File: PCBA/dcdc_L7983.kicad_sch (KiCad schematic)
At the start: 13 parts

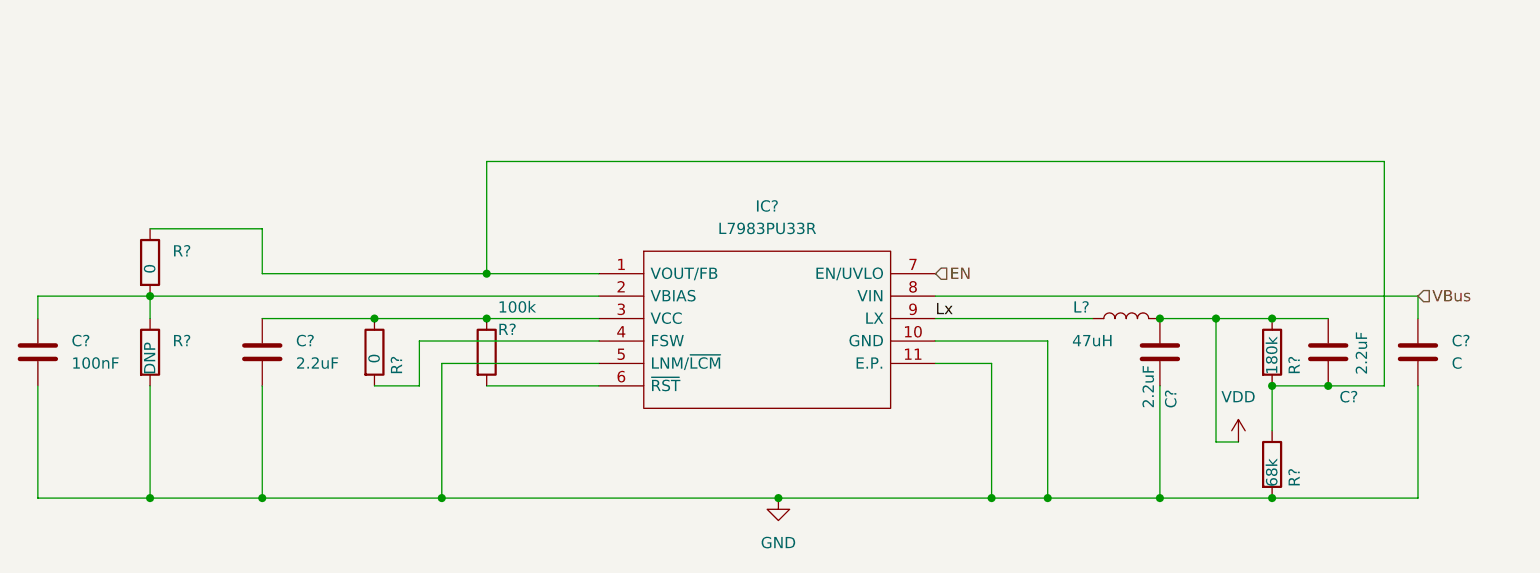
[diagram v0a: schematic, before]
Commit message: Assign footprints
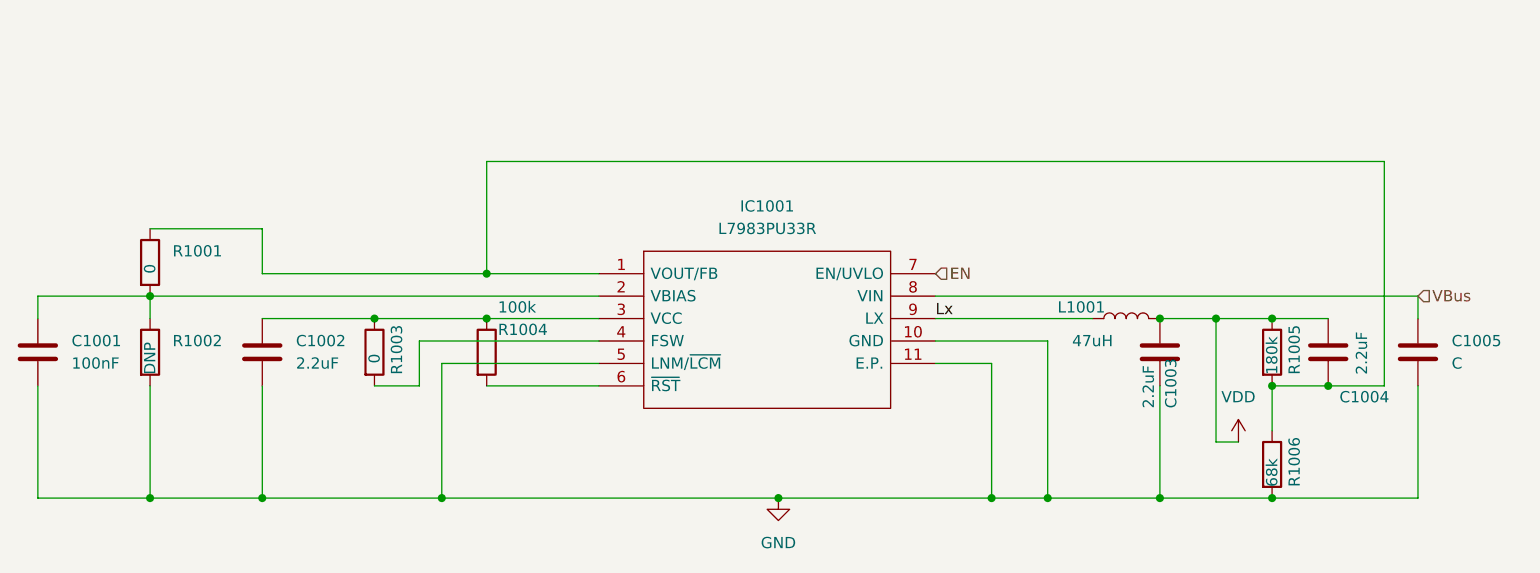
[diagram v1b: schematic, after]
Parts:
- C1001, C1002, C1003, C1004, C1005: renamed from C?; footprint (none) -> Capacitor_SMD:C_0603_1608Metric
- IC1001: renamed from IC?; footprint L7983PU33R -> L7983PU33R:L7983PU33R
- R1001, R1002, R1003, R1004, R1005, R1006: renamed from R?; footprint (none) -> Resistor_SMD:R_0603_1608Metric
- gave numbers to parts that had none: 1
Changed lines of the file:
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@@
   (symbol (lib_id "Device:L") (at 176.53 92.71 90) (unit 1)
     (in_bom yes) (on_board yes)
-    (property "Reference" "L?" (id 0) (at 171.45 91.44 90))
+    (property "Reference" "L1001" (id 0) (at 171.45 91.44 90))
     (property "Value" "47uH" (id 1) (at 172.72 95.25 90))
     (property "Footprint" "" (id 2) (at 176.53 92.71 0)
@@
   (symbol (lib_id "Device:R") (at 193.04 109.22 0) (unit 1)
     (in_bom yes) (on_board yes)
-    (property "Reference" "R?" (id 0) (at 195.58 111.76 90)
+    (property "Reference" "R1006" (id 0) (at 195.58 111.76 90)
       (effects (font (size 1.27 1.27)) (justify left))
     )
@@
       (effects (font (size 1.27 1.27)) (justify left))
     )
-    (property "Footprint" "" (id 2) (at 191.262 109.22 90)
+    (property "Footprint" "Resistor_SMD:R_0603_1608Metric" (id 2) (at 191.262 109.22 90)
       (effects (font (size 1.27 1.27)) hide)
     )
@@
   (symbol (lib_id "Device:R") (at 104.14 96.52 0) (unit 1)
     (in_bom yes) (on_board yes)
-    (property "Reference" "R?" (id 0) (at 105.41 93.98 0)
+    (property "Reference" "R1004" (id 0) (at 105.41 93.98 0)
       (effects (font (size 1.27 1.27)) (justify left))
     )
@@
       (effects (font (size 1.27 1.27)) (justify left))
     )
-    (property "Footprint" "" (id 2) (at 102.362 96.52 90)
+    (property "Footprint" "Resistor_SMD:R_0603_1608Metric" (id 2) (at 102.362 96.52 90)
       (effects (font (size 1.27 1.27)) hide)
     )
@@
   (symbol (lib_id "Device:R") (at 66.04 96.52 0) (unit 1)
     (in_bom yes) (on_board yes)
-    (property "Reference" "R?" (id 0) (at 68.58 95.2499 0)
+    (property "Reference" "R1002" (id 0) (at 68.58 95.2499 0)
       (effects (font (size 1.27 1.27)) (justify left))
     )
@@
       (effects (font (size 1.27 1.27)) (justify left))
     )
-    (property "Footprint" "" (id 2) (at 64.262 96.52 90)
+    (property "Footprint" "Resistor_SMD:R_0603_1608Metric" (id 2) (at 64.262 96.52 90)
       (effects (font (size 1.27 1.27)) hide)
     )
@@
   (symbol (lib_id "Device:C") (at 209.55 96.52 0) (unit 1)
     (in_bom yes) (on_board yes) (fields_autoplaced)
-    (property "Reference" "C?" (id 0) (at 213.36 95.2499 0)
+    (property "Reference" "C1005" (id 0) (at 213.36 95.2499 0)
       (effects (font (size 1.27 1.27)) (justify left))
     )
@@
       (effects (font (size 1.27 1.27)) (justify left))
     )
-    (property "Footprint" "" (id 2) (at 210.5152 100.33 0)
+    (property "Footprint" "Capacitor_SMD:C_0603_1608Metric" (id 2) (at 210.5152 100.33 0)
       (effects (font (size 1.27 1.27)) hide)
     )
@@
   (symbol (lib_id "Device:R") (at 91.44 96.52 0) (unit 1)
     (in_bom yes) (on_board yes)
-    (property "Reference" "R?" (id 0) (at 93.98 99.06 90)
+    (property "Reference" "R1003" (id 0) (at 93.98 99.06 90)
       (effects (font (size 1.27 1.27)) (justify left))
     )
@@
       (effects (font (size 1.27 1.27)) (justify left))
     )
-    (property "Footprint" "" (id 2) (at 89.662 96.52 90)
+    (property "Footprint" "Resistor_SMD:R_0603_1608Metric" (id 2) (at 89.662 96.52 90)
       (effects (font (size 1.27 1.27)) hide)
     )
@@
   (symbol (lib_id "Device:R") (at 193.04 96.52 0) (unit 1)
     (in_bom yes) (on_board yes)
-    (property "Reference" "R?" (id 0) (at 195.58 99.06 90)
+    (property "Reference" "R1005" (id 0) (at 195.58 99.06 90)
       (effects (font (size 1.27 1.27)) (justify left))
     )
@@
       (effects (font (size 1.27 1.27)) (justify left))
     )
-    (property "Footprint" "" (id 2) (at 191.262 96.52 90)
+    (property "Footprint" "Resistor_SMD:R_0603_1608Metric" (id 2) (at 191.262 96.52 90)
       (effects (font (size 1.27 1.27)) hide)
     )
@@
   (symbol (lib_id "Device:C") (at 78.74 96.52 0) (unit 1)
     (in_bom yes) (on_board yes) (fields_autoplaced)
-    (property "Reference" "C?" (id 0) (at 82.55 95.2499 0)
+    (property "Reference" "C1002" (id 0) (at 82.55 95.2499 0)
       (effects (font (size 1.27 1.27)) (justify left))
     )
@@
       (effects (font (size 1.27 1.27)) (justify left))
     )
-    (property "Footprint" "" (id 2) (at 79.7052 100.33 0)
+    (property "Footprint" "Capacitor_SMD:C_0603_1608Metric" (id 2) (at 79.7052 100.33 0)
       (effects (font (size 1.27 1.27)) hide)
     )
@@
   (symbol (lib_id "Device:R") (at 66.04 86.36 0) (unit 1)
     (in_bom yes) (on_board yes)
-    (property "Reference" "R?" (id 0) (at 68.58 85.0899 0)
+    (property "Reference" "R1001" (id 0) (at 68.58 85.0899 0)
       (effects (font (size 1.27 1.27)) (justify left))
     )
@@
       (effects (font (size 1.27 1.27)) (justify left))
     )
-    (property "Footprint" "" (id 2) (at 64.262 86.36 90)
+    (property "Footprint" "Resistor_SMD:R_0603_1608Metric" (id 2) (at 64.262 86.36 90)
       (effects (font (size 1.27 1.27)) hide)
     )
@@
   (symbol (lib_id "power:VDD") (at 189.23 106.68 0) (unit 1)
     (in_bom yes) (on_board yes) (fields_autoplaced)
-    (property "Reference" "#PWR?" (id 0) (at 189.23 110.49 0)
+    (property "Reference" "#PWR0158" (id 0) (at 189.23 110.49 0)
       (effects (font (size 1.27 1.27)) hide)
     )
@@
   (symbol (lib_id "power:GND") (at 137.16 113.03 0) (unit 1)
     (in_bom yes) (on_board yes) (fields_autoplaced)
-    (property "Reference" "#PWR?" (id 0) (at 137.16 119.38 0)
+    (property "Reference" "#PWR0157" (id 0) (at 137.16 119.38 0)
       (effects (font (size 1.27 1.27)) hide)
     )
@@
   (symbol (lib_id "Device:C") (at 53.34 96.52 0) (unit 1)
     (in_bom yes) (on_board yes) (fields_autoplaced)
-    (property "Reference" "C?" (id 0) (at 57.15 95.2499 0)
+    (property "Reference" "C1001" (id 0) (at 57.15 95.2499 0)
       (effects (font (size 1.27 1.27)) (justify left))
     )
@@
       (effects (font (size 1.27 1.27)) (justify left))
     )
-    (property "Footprint" "" (id 2) (at 54.3052 100.33 0)
+    (property "Footprint" "Capacitor_SMD:C_0603_1608Metric" (id 2) (at 54.3052 100.33 0)
       (effects (font (size 1.27 1.27)) hide)
     )
@@
   (symbol (lib_id "Device:C") (at 180.34 96.52 0) (unit 1)
     (in_bom yes) (on_board yes)
-    (property "Reference" "C?" (id 0) (at 181.61 102.87 90)
+    (property "Reference" "C1003" (id 0) (at 181.61 102.87 90)
       (effects (font (size 1.27 1.27)) (justify left))
     )
@@
       (effects (font (size 1.27 1.27)) (justify left))
     )
-    (property "Footprint" "" (id 2) (at 181.3052 100.33 0)
+    (property "Footprint" "Capacitor_SMD:C_0603_1608Metric" (id 2) (at 181.3052 100.33 0)
       (effects (font (size 1.27 1.27)) hide)
     )
@@
   (symbol (lib_id "Device:C") (at 199.39 96.52 0) (unit 1)
     (in_bom yes) (on_board yes)
-    (property "Reference" "C?" (id 0) (at 200.66 101.6 0)
+    (property "Reference" "C1004" (id 0) (at 200.66 101.6 0)
       (effects (font (size 1.27 1.27)) (justify left))
     )
@@
       (effects (font (size 1.27 1.27)) (justify left))
     )
-    (property "Footprint" "" (id 2) (at 200.3552 100.33 0)
+    (property "Footprint" "Capacitor_SMD:C_0603_1608Metric" (id 2) (at 200.3552 100.33 0)
       (effects (font (size 1.27 1.27)) hide)
     )
@@
   (symbol (lib_id "L7983PU33R:L7983PU33R") (at 116.84 87.63 0) (unit 1)
     (in_bom yes) (on_board yes) (fields_autoplaced)
-    (property "Reference" "IC?" (id 0) (at 135.89 80.01 0))
+    (property "Reference" "IC1001" (id 0) (at 135.89 80.01 0))
     (property "Value" "L7983PU33R" (id 1) (at 135.89 82.55 0))
-    (property "Footprint" "L7983PU33R" (id 2) (at 151.13 85.09 0)
+    (property "Footprint" "L7983PU33R:L7983PU33R" (id 2) (at 151.13 85.09 0)
       (effects (font (size 1.27 1.27)) (justify left) hide)
     )

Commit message: Rough outline
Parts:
- L1001: footprint (none) -> Inductor_SMD:L_Taiyo-Yuden_NR-40xx_HandSoldering
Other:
- note added: "https://lcsc.com/product-detail/Inductors-SMD_SHOU-HAN-CY43-47UH_C2929422.html"
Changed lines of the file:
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@@
     (stroke (width 0) (type default) (color 0 0 0 0))
+  )
+  (text "https://lcsc.com/product-detail/Inductors-SMD_SHOU-HAN-CY43-47UH_C2929422.html"
+    (at 116.84 60.96 0)
+    (effects (font (size 1.27 1.27)) (justify left bottom))
   )
   (label "Lx" (at 154.94 92.71 0)
@@
     (property "Reference" "L1001" (id 0) (at 171.45 91.44 90))
     (property "Value" "47uH" (id 1) (at 172.72 95.25 90))
-    (property "Footprint" "" (id 2) (at 176.53 92.71 0)
+    (property "Footprint" "Inductor_SMD:L_Taiyo-Yuden_NR-40xx_HandSoldering" (id 2) (at 176.53 92.71 0)
       (effects (font (size 1.27 1.27)) hide)
     )

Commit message: Routing
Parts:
- L1001: footprint Inductor_SMD:L_Taiyo-Yuden_NR-40xx_HandSoldering -> Inductor_SMD:L_1210_3225Metric
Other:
- note added: "https://www.lcsc.com/product-detail/Inductors-SMD_TDK-NLCV32T-470K-PF_C83083.html"
- note removed: "https://lcsc.com/product-detail/Inductors-SMD_SHOU-HAN-CY43-47UH_C2929422.html"
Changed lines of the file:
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@@
     (stroke (width 0) (type default) (color 0 0 0 0))
   )
-  (text "https://lcsc.com/product-detail/Inductors-SMD_SHOU-HAN-CY43-47UH_C2929422.html"
+  (text "https://www.lcsc.com/product-detail/Inductors-SMD_TDK-NLCV32T-470K-PF_C83083.html"
     (at 116.84 60.96 0)
     (effects (font (size 1.27 1.27)) (justify left bottom))
@@
     (property "Reference" "L1001" (id 0) (at 171.45 91.44 90))
     (property "Value" "47uH" (id 1) (at 172.72 95.25 90))
-    (property "Footprint" "Inductor_SMD:L_Taiyo-Yuden_NR-40xx_HandSoldering" (id 2) (at 176.53 92.71 0)
+    (property "Footprint" "Inductor_SMD:L_1210_3225Metric" (id 2) (at 176.53 92.71 0)
       (effects (font (size 1.27 1.27)) hide)
     )

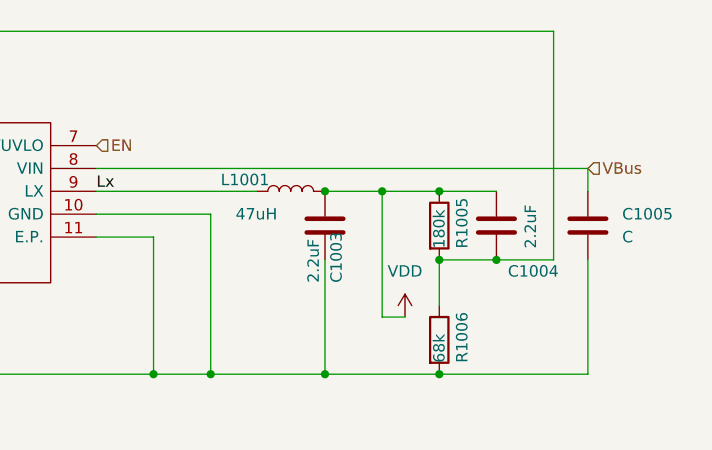
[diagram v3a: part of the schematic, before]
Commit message: Step models for ports
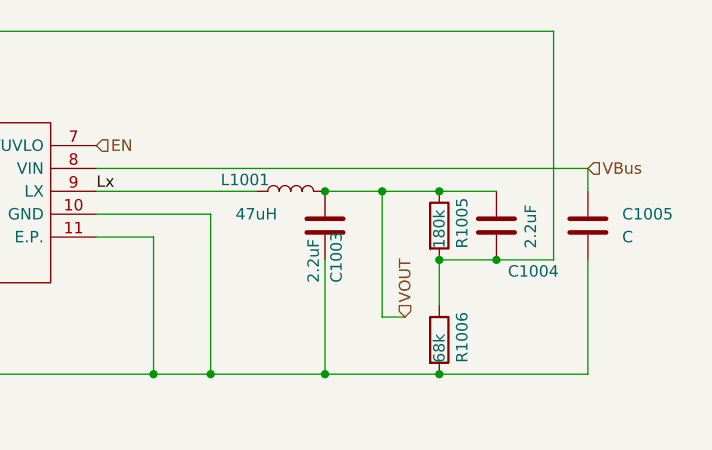
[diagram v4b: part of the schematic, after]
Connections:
- net VDD renamed VOUT
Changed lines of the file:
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@@
+    (effects (font (size 1.27 1.27)) (justify left))
+  )
+  (hierarchical_label "VOUT" (shape input) (at 189.23 106.68 90)
     (effects (font (size 1.27 1.27)) (justify left))
   )
@@
     (pin "2")
   )
-  (symbol (lib_id "power:VDD") (at 189.23 106.68 0) (unit 1)
-    (in_bom yes) (on_board yes) (fields_autoplaced)
-    (property "Reference" "#PWR0158" (id 0) (at 189.23 110.49 0)
-      (effects (font (size 1.27 1.27)) hide)
-    )
-    (property "Value" "VDD" (id 1) (at 189.23 101.6 0))
-    (property "Footprint" "" (id 2) (at 189.23 106.68 0)
-      (effects (font (size 1.27 1.27)) hide)
-    )
-    (property "Datasheet" "" (id 3) (at 189.23 106.68 0)
-      (effects (font (size 1.27 1.27)) hide)
-    )
-    (pin "1")
-  )
   (symbol (lib_id "power:GND") (at 137.16 113.03 0) (unit 1)
